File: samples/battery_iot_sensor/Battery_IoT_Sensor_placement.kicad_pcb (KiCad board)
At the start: 2 copper layers, 63 x 70 mm, 5 parts, among them J1 USB-C, U1 MCP73831T-2ACI/OT, U2 MAX17048G+T, U3 TLV75518, U4 ESP32-WROOM-32E

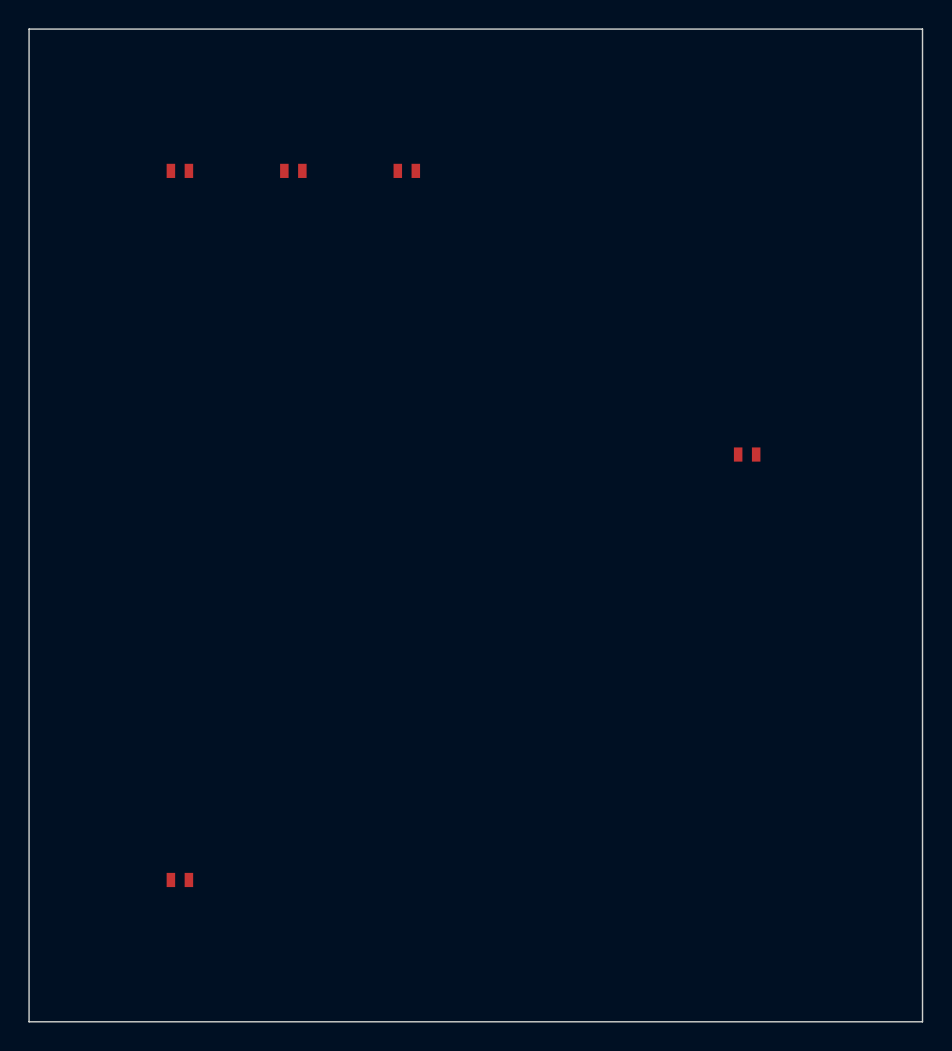
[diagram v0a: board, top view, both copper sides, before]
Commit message: chore: regenerate 8 sample designs against v0.27.0 engine
All 8 samples pass full validation (0 ERC errors):
- led_power_indicator, iot_sensor_node, usb_regulated_supply,
  usb_uart_bridge, oled_display_module, battery_iot_sensor,
  motor_controller, fpga_power_carrier

New artifacts per sample: .kicad_sch, _test_points.csv, _pinout.csv,
canonical_spec.yaml, design_ir.json, validation_report.json; MCU samples
also emit sdkconfig.defaults / .ioc stubs.

Also adds samples/*/svg/ to .gitignore — schematic SVG exports are
regenerable and too large to track.

zigbee_humidistat deferred: non-deterministic schematic output across
two generation runs (text annotation ordering vs sheet_instances).
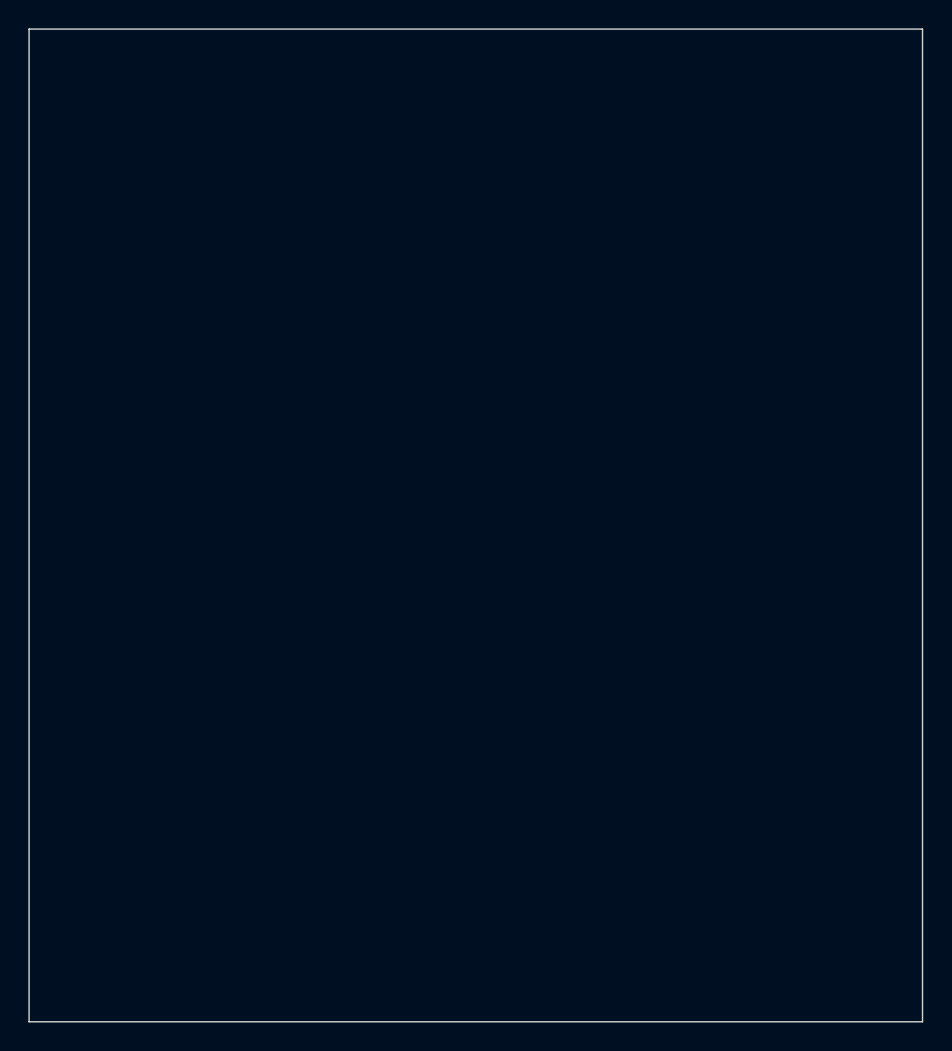
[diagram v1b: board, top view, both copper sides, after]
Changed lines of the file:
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@@
-(kicad_pcb (version 20240108) (generator "schematic_engine")
+(kicad_pcb (version 20240108) (generator "schematic_engine placement_preview")
   (general (thickness 1.6) (legacy_teardrops no))
   (layers
@@
       (effects (font (size 1.0 1.0) (thickness 0.15)))
     )
-    (pad "1" smd rect (at 0.00 0) (size 0.6 1.0) (layers "F.Cu" "F.Paste" "F.Mask") (net 17 "VUSB_5V"))
-    (pad "2" smd rect (at 1.27 0) (size 0.6 1.0) (layers "F.Cu" "F.Paste" "F.Mask") (net 4 "GND"))
   )
   (footprint "DFN-8-EP"
@@
       (effects (font (size 1.0 1.0) (thickness 0.15)))
     )
-    (pad "1" smd rect (at 0.00 0) (size 0.6 1.0) (layers "F.Cu" "F.Paste" "F.Mask") (net 14 "VBAT"))
-    (pad "2" smd rect (at 1.27 0) (size 0.6 1.0) (layers "F.Cu" "F.Paste" "F.Mask") (net 4 "GND"))
   )
   (footprint "SOT-23-5"
@@
       (effects (font (size 1.0 1.0) (thickness 0.15)))
     )
-    (pad "1" smd rect (at 0.00 0) (size 0.6 1.0) (layers "F.Cu" "F.Paste" "F.Mask") (net 14 "VBAT"))
-    (pad "2" smd rect (at 1.27 0) (size 0.6 1.0) (layers "F.Cu" "F.Paste" "F.Mask") (net 4 "GND"))
   )
   (footprint "RF_Module:ESP32-WROOM-32E"
@@
       (effects (font (size 1.0 1.0) (thickness 0.15)))
     )
-    (pad "1" smd rect (at 0.00 0) (size 0.6 1.0) (layers "F.Cu" "F.Paste" "F.Mask") (net 4 "GND"))
-    (pad "2" smd rect (at 1.27 0) (size 0.6 1.0) (layers "F.Cu" "F.Paste" "F.Mask") (net 16 "VDD_3P3"))
   )
   (footprint "Connector_USB:USB_C_Receptacle_GCT_USB4085"
@@
       (effects (font (size 1.0 1.0) (thickness 0.15)))
     )
-    (pad "1" smd rect (at 0.00 0) (size 0.6 1.0) (layers "F.Cu" "F.Paste" "F.Mask") (net 15 "VBUS_5V"))
-    (pad "2" smd rect (at 1.27 0) (size 0.6 1.0) (layers "F.Cu" "F.Paste" "F.Mask") (net 4 "GND"))
   )
   (gr_line (start 0.00 0.00) (end 63.00 0.00) (stroke (width 0.1) (type solid)) (layer "Edge.Cuts"))
